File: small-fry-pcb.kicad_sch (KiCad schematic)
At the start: 139 parts, among them U1 Pico

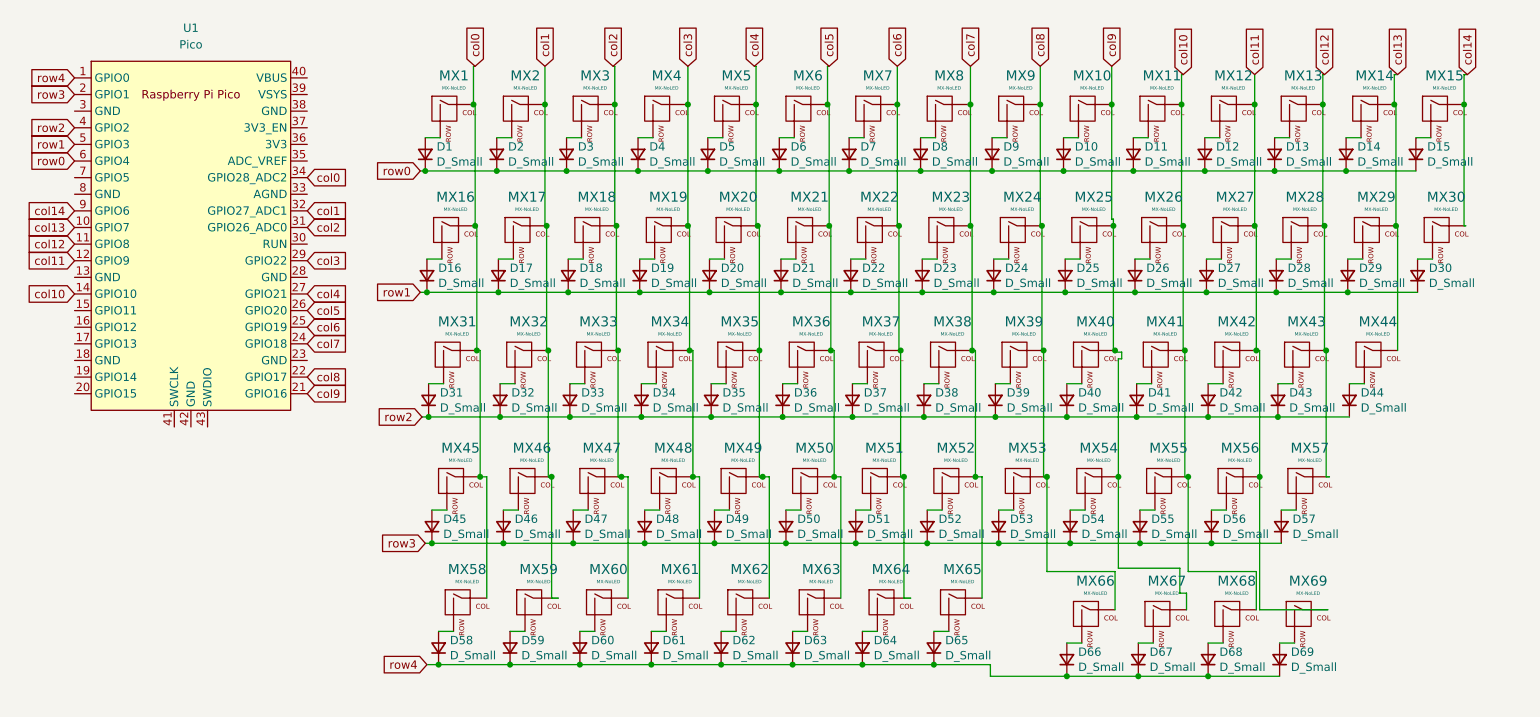
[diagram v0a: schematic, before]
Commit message: updated matrix routing
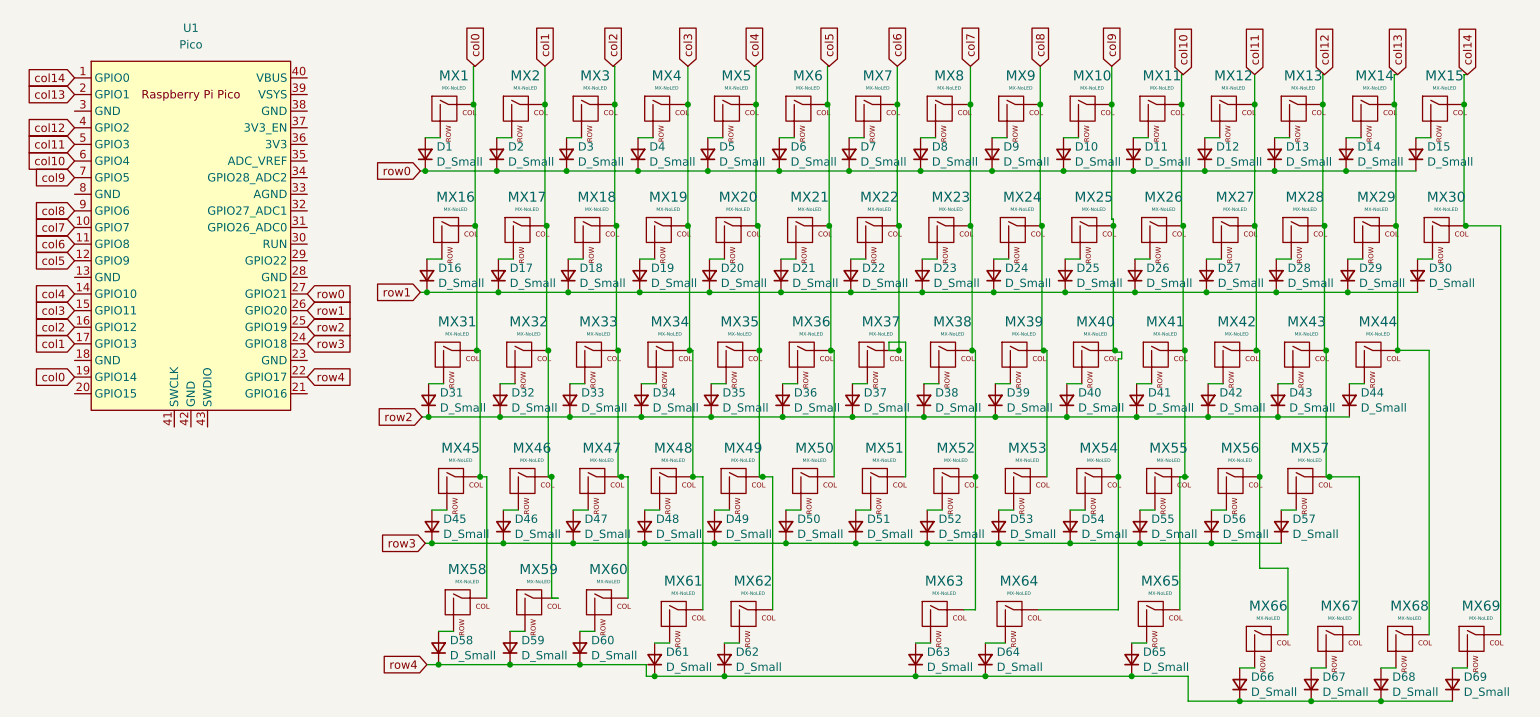
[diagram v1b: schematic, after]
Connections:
- net col0: now also U1.19 (GPIO14); no longer U1.34 (GPIO28_ADC2)
- net col1: now also U1.17 (GPIO13); no longer U1.32 (GPIO27_ADC1)
- net col10: now also MX65.1 (COL), U1.6 (GPIO4); no longer MX68.1 (COL), U1.14 (GPIO10)
- net col11: now also MX66.1 (COL), U1.5 (GPIO3); no longer MX69.1 (COL), U1.12 (GPIO9)
- net col12: now also MX67.1 (COL), U1.4 (GPIO2); no longer U1.11 (GPIO8)
- net col13: now also MX68.1 (COL), U1.2 (GPIO1); no longer U1.10 (GPIO7)
- net col14: now also MX69.1 (COL), U1.1 (GPIO0); no longer U1.9 (GPIO6)
- net col2: now also U1.16 (GPIO12); no longer U1.31 (GPIO26_ADC0)
- net col3: now also U1.15 (GPIO11); no longer U1.29 (GPIO22)
- net col4: now also U1.14 (GPIO10); no longer U1.27 (GPIO21)
- net col5: now also U1.12 (GPIO9); no longer MX63.1 (COL), U1.26 (GPIO20)
- net col6: now also U1.11 (GPIO8); no longer MX64.1 (COL), U1.25 (GPIO19)
- net col7: now also MX63.1 (COL), U1.10 (GPIO7); no longer MX65.1 (COL), U1.24 (GPIO18)
- net col8: now also U1.9 (GPIO6); no longer MX66.1 (COL), U1.22 (GPIO17)
- net col9: now also MX64.1 (COL), U1.7 (GPIO5); no longer MX67.1 (COL), U1.21 (GPIO16)
- net row0: now also U1.27 (GPIO21); no longer U1.6 (GPIO4)
- net row1: now also U1.26 (GPIO20); no longer U1.5 (GPIO3)
- net row2: now also U1.25 (GPIO19); no longer U1.4 (GPIO2)
- net row3: now also U1.24 (GPIO18); no longer U1.2 (GPIO1)
- net row4: now also U1.22 (GPIO17); no longer U1.1 (GPIO0)
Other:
- moved on the sheet: D61, D62, D63, D64, D65, D66, D67, D68, D69, MX61, MX62, MX63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

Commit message: changed mods, changed col stagger
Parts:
- MX1, MX16, MX31, MX45, MX58: footprint MX_Alps_Hybrid:MX-1.75U-NoLED -> MX_Alps_Hybrid:MX-1.25U-NoLED
- MX15, MX17, MX2, MX30, MX32, MX44, MX46, MX57, MX59: footprint MX_Alps_Hybrid:MX-1.75U-NoLED -> MX_Alps_Hybrid:MX-1.5U-NoLED
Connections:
- net col4: no longer MX62.1 (COL)
- net col5: now also MX62.1 (COL)
- net col7: no longer MX63.1 (COL)
- net col8: now also MX63.1 (COL)
- no-connect marks 0 -> 23
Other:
- moved on the sheet: D63, D64, MX63, MX64

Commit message: changed footprints, rerouted
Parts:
- MX1, MX16, MX31, MX45, MX58: footprint MX_Alps_Hybrid:MX-1.25U-NoLED -> marbastlib-mx:SW_MX_1.25u
- MX10, MX11, MX12, MX13, MX14, MX18, MX19, MX20, MX21, MX22, MX23, MX24, MX25, MX26, MX27, MX28, MX29, MX3, MX33, MX34, MX35, MX36, MX37, MX38, MX39, MX4, MX40, MX41, MX42, MX43, MX47, MX48, MX49, MX5, MX50, MX51, MX52, MX53, MX54, MX55, MX56, MX6, MX60, MX61, MX64, MX65, MX66, MX67, MX68, MX69, MX7, MX8, MX9: footprint MX_Alps_Hybrid:MX-1U-NoLED -> marbastlib-mx:SW_MX_1u
- MX15, MX17, MX2, MX30, MX32, MX44, MX46, MX57, MX59: footprint MX_Alps_Hybrid:MX-1.5U-NoLED -> marbastlib-mx:SW_MX_1.5u
- MX62: footprint MX_Alps_Hybrid:MX-2.25U-ReversedStabilizers-NoLED -> MX_Solderable:MX-Solderable-2.25U-ReversedStabilizers
- MX63: footprint MX_Alps_Hybrid:MX-2.75U-ReversedStabilizers-NoLED -> MX_Solderable:MX-Solderable-2.75U-ReversedStabilizers
